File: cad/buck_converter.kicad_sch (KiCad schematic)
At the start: 5 parts, among them Q1 SW

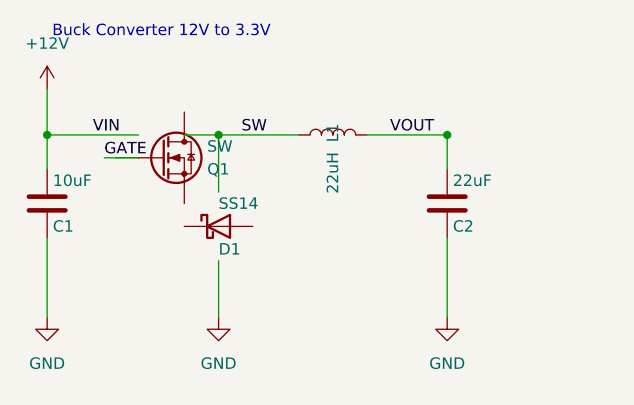
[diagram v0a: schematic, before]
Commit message: ✨ feat: align poe tasks, fix ERC, add ISO title block with logo
Rename poe tasks for symmetry: inspect→inspect-model, export→drawings,
validate→validate-model. Add inspect-asm for pcbnew. Fix all 16 ERC
violations by correcting schematic wiring and adding PWR_FLAG symbols.
Custom ISO 7200 drawing sheet with EWAI logo, approval chain. SVG
exports circuit-only for web, PDF includes full title block. Fix lint
errors (unused imports, ambiguous var names, notebook naming).

Co-Authored-By: Claude Opus 4.6 (1M context) <noreply@anthropic.com>
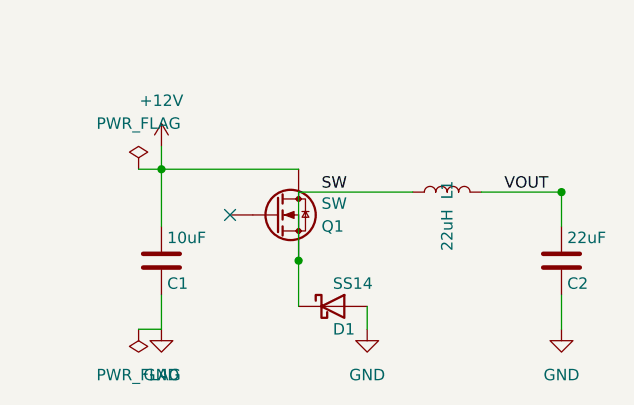
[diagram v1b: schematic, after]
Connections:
- net +12V: now also Q1.D
- net GND: now also D1.2 (A)
- net SW: now also D1.1 (K), Q1.S
- no-connect marks 0 -> 1
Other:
- note removed: "Buck Converter 12V to 3.3V"
- company: (none) -> Engineering With AI
- title: Buck_Converter -> Buck Converter 12V to 3.3V

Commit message: 🔧 fix: use 2N7002 symbol for correct SOT-23 pin mapping
Device:Q_NMOS uses pin numbers G/D/S which don't match SOT-23 pad
numbers 1/2/3. Switched to Transistor_FET:2N7002 (extends Q_NMOS_GSD)
which maps G→1, S→2, D→3. PCB import now works. Added footprints to
schematic components. inspect-asm opens project manager for pcbnew
context.

Co-Authored-By: Claude Opus 4.6 (1M context) <noreply@anthropic.com>
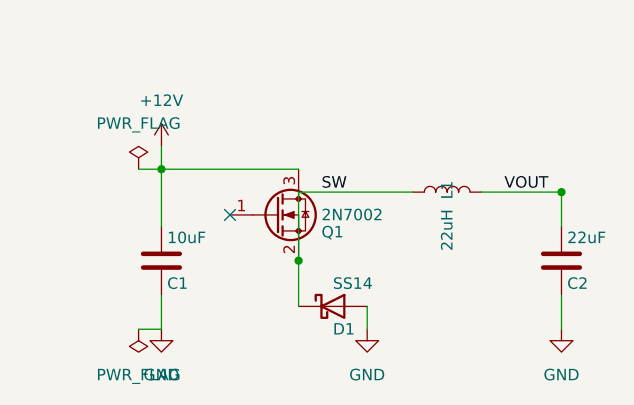
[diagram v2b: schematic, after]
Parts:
- removed Q1: SW, symbol Device:Q_NMOS
- added Q1: 2N7002, Package_TO_SOT_SMD:SOT-23, symbol Transistor_FET:2N7002
- C1, C2: footprint (none) -> Capacitor_SMD:C_0805_2012Metric
- D1: footprint (none) -> Diode_SMD:D_SOD-123
- L1: footprint (none) -> Inductor_SMD:L_1210_3225Metric
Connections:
- net +12V: now also Q1.3 (D)
- net SW: now also Q1.2 (S)
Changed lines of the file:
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@@
 		(instances
 			(project "Buck_Converter"
-				(path "/368e062f-dc81-4c93-8406-d3172110318e"
+				(path "/6bd2aa9d-cafa-4aaf-a12b-3f11ce2c3414"
 					(reference "#PWR01")
 					(unit 1)
@@
 		(instances
 			(project "Buck_Converter"
-				(path "/368e062f-dc81-4c93-8406-d3172110318e"
+				(path "/6bd2aa9d-cafa-4aaf-a12b-3f11ce2c3414"
 					(reference "#PWR02")
 					(unit 1)
@@
 		(instances
 			(project "Buck_Converter"
-				(path "/368e062f-dc81-4c93-8406-d3172110318e"
+				(path "/6bd2aa9d-cafa-4aaf-a12b-3f11ce2c3414"
 					(reference "#PWR03")
 					(unit 1)
@@
 		(instances
 			(project "Buck_Converter"
-				(path "/368e062f-dc81-4c93-8406-d3172110318e"
+				(path "/6bd2aa9d-cafa-4aaf-a12b-3f11ce2c3414"
 					(reference "#PWR04")
 					(unit 1)
@@
 		(instances
 			(project "Buck_Converter"
-				(path "/368e062f-dc81-4c93-8406-d3172110318e"
+				(path "/6bd2aa9d-cafa-4aaf-a12b-3f11ce2c3414"
 					(reference "#FLG01")
 					(unit 1)
@@
 		(instances
 			(project "Buck_Converter"
-				(path "/368e062f-dc81-4c93-8406-d3172110318e"
+				(path "/6bd2aa9d-cafa-4aaf-a12b-3f11ce2c3414"
 					(reference "#FLG02")
 					(unit 1)
@@
 			)
 		)
+		(property "Footprint" "Capacitor_SMD:C_0805_2012Metric"
+			(at 39.0652 40.64 0.0000)
+			(effects
+				(font
+					(size 1.27 1.27)
+				)
+				(hide yes)
+			)
+		)
 		(pin "1"
 		)
@@
 		(instances
 			(project "Buck_Converter"
-				(path "/368e062f-dc81-4c93-8406-d3172110318e"
+				(path "/6bd2aa9d-cafa-4aaf-a12b-3f11ce2c3414"
 					(reference "C1")
 					(unit 1)
@@
 	)
 	(symbol
-		(lib_id "Device:Q_NMOS")
+		(lib_id "Transistor_FET:2N7002")
 		(at 50.8 39.37 0)
 		(unit 1)
@@
 		(fields_autoplaced no)
 		(property "Reference" "Q1"
-			(at 55.88 40.64 0.0000)
-			(effects
-				(font
-					(size 1.27 1.27)
-				)
-				(justify left)
-			)
-		)
-		(property "Value" "SW"
-			(at 55.88 38.1 0.0000)
-			(effects
-				(font
-					(size 1.27 1.27)
-				)
-				(justify left)
-			)
-		)
-		(pin "G"
-		)
-		(pin "D"
-		)
-		(pin "S"
-		)
-		(instances
-			(project "Buck_Converter"
-				(path "/368e062f-dc81-4c93-8406-d3172110318e"
+			(at 55.88 41.275 0.0000)
+			(effects
+				(font
+					(size 1.27 1.27)
+				)
+				(justify left)
+			)
+		)
+		(property "Value" "2N7002"
+			(at 55.88 39.37 0.0000)
+			(effects
+				(font
+					(size 1.27 1.27)
+				)
+				(justify left)
+			)
+		)
+		(property "Footprint" "Package_TO_SOT_SMD:SOT-23"
+			(at 55.88 37.465 0.0000)
+			(effects
+				(font
+					(size 1.27 1.27)
+				)
+				(hide yes)
+			)
+		)
+		(pin "1"
+		)
+		(pin "3"
+		)
+		(pin "2"
+		)
+		(instances
+			(project "Buck_Converter"
+				(path "/6bd2aa9d-cafa-4aaf-a12b-3f11ce2c3414"
 					(reference "Q1")
 					(unit 1)
@@
 			)
 		)
+		(property "Footprint" "Diode_SMD:D_SOD-123"
+			(at 57.15 49.53 0.0000)
+			(effects
+				(font
+					(size 1.27 1.27)
+				)
+				(hide yes)
+			)
+		)
 		(pin "1"
 		)
@@
 		(instances
 			(project "Buck_Converter"
-				(path "/368e062f-dc81-4c93-8406-d3172110318e"
+				(path "/6bd2aa9d-cafa-4aaf-a12b-3f11ce2c3414"
 					(reference "D1")
 					(unit 1)
@@
 			)
 		)
+		(property "Footprint" "Inductor_SMD:L_1210_3225Metric"
+			(at 69.85 36.83 0.0000)
+			(effects
+				(font
+					(size 1.27 1.27)
+				)
+				(hide yes)
+			)
+		)
 		(pin "1"
 		)
@@
 		(instances
 			(project "Buck_Converter"
-				(path "/368e062f-dc81-4c93-8406-d3172110318e"
+				(path "/6bd2aa9d-cafa-4aaf-a12b-3f11ce2c3414"
 					(reference "L1")
 					(unit 1)
@@
 			)
 		)
+		(property "Footprint" "Capacitor_SMD:C_0805_2012Metric"
+			(at 83.5152 40.64 0.0000)
+			(effects
+				(font
+					(size 1.27 1.27)
+				)
+				(hide yes)
+			)
+		)
 		(pin "1"
 		)
@@
 		(instances
 			(project "Buck_Converter"
-				(path "/368e062f-dc81-4c93-8406-d3172110318e"
+				(path "/6bd2aa9d-cafa-4aaf-a12b-3f11ce2c3414"
 					(reference "C2")
 					(unit 1)
